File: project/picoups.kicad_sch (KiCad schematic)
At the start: 21 parts, among them J1 Conn_02x20_Odd_Even, J2 Conn_01x02, J3 Conn_01x02, SW1 SW_Push

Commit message: Cleanup
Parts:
- removed C1: 1uF, Capacitor_SMD:C_0603_1608Metric, symbol Device:C
- removed C2, C4: 22uF, Capacitor_SMD:C_0805_2012Metric, symbol Device:C
- removed C3: 47nF, Capacitor_SMD:C_0603_1608Metric, symbol Device:C
- removed C5, C6: 10uF, Capacitor_SMD:C_0603_1608Metric, symbol Device:C
- removed D1: LED, LED_SMD:LED_0805_2012Metric, symbol Device:LED
- removed J2, J3: Conn_01x02, Connector_JST:JST_PH_S2B-PH-K_1x02_P2.00mm_Horizontal, symbol Connector_Generic:Conn_01x02
- removed L1: 10uH, PicoUPS:Inductor, symbol Device:L
- removed R1: 240k, Resistor_SMD:R_0201_0603Metric, symbol Device:R
- removed R2, R3: R, Resistor_SMD:R_0201_0603Metric, symbol Device:R
- removed R4, R5: 10k, Resistor_SMD:R_0201_0603Metric, symbol Device:R
- removed SW1: SW_Push, Button_Switch_SMD:SW_Push_1P1T_NO_Vertical_Wuerth_434133025816, symbol Switch:SW_Push
- removed TH1: Thermistor_NTC, Connector_PinHeader_2.54mm:PinHeader_1x02_P2.54mm_Vertical, symbol Device:Thermistor_NTC
- removed TP1: DP, TestPoint:TestPoint_Pad_D1.5mm, symbol Connector:TestPoint
- removed TP2: DM, TestPoint:TestPoint_Pad_D1.5mm, symbol Connector:TestPoint
- removed U2: ~, PicoUPS:MP2731, symbol PicoUPS:MP2731
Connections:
- removed net GNDA: J1.14 (Pin_14), J1.20 (Pin_20), J1.25 (Pin_25), J1.30 (Pin_30), J1.34 (Pin_34), J1.39 (Pin_39), J1.6 (Pin_6), J1.9 (Pin_9)
- net INT: no longer names the net of J1.11 (Pin_11)
- net OTG: no longer names the net of J1.15 (Pin_15)
- net SCL: no longer names the net of J1.5 (Pin_5)
- net SDA: no longer names the net of J1.3 (Pin_3)
- net ~{CE}: no longer names the net of J1.13 (Pin_13)
- no-connect marks 27 -> 0

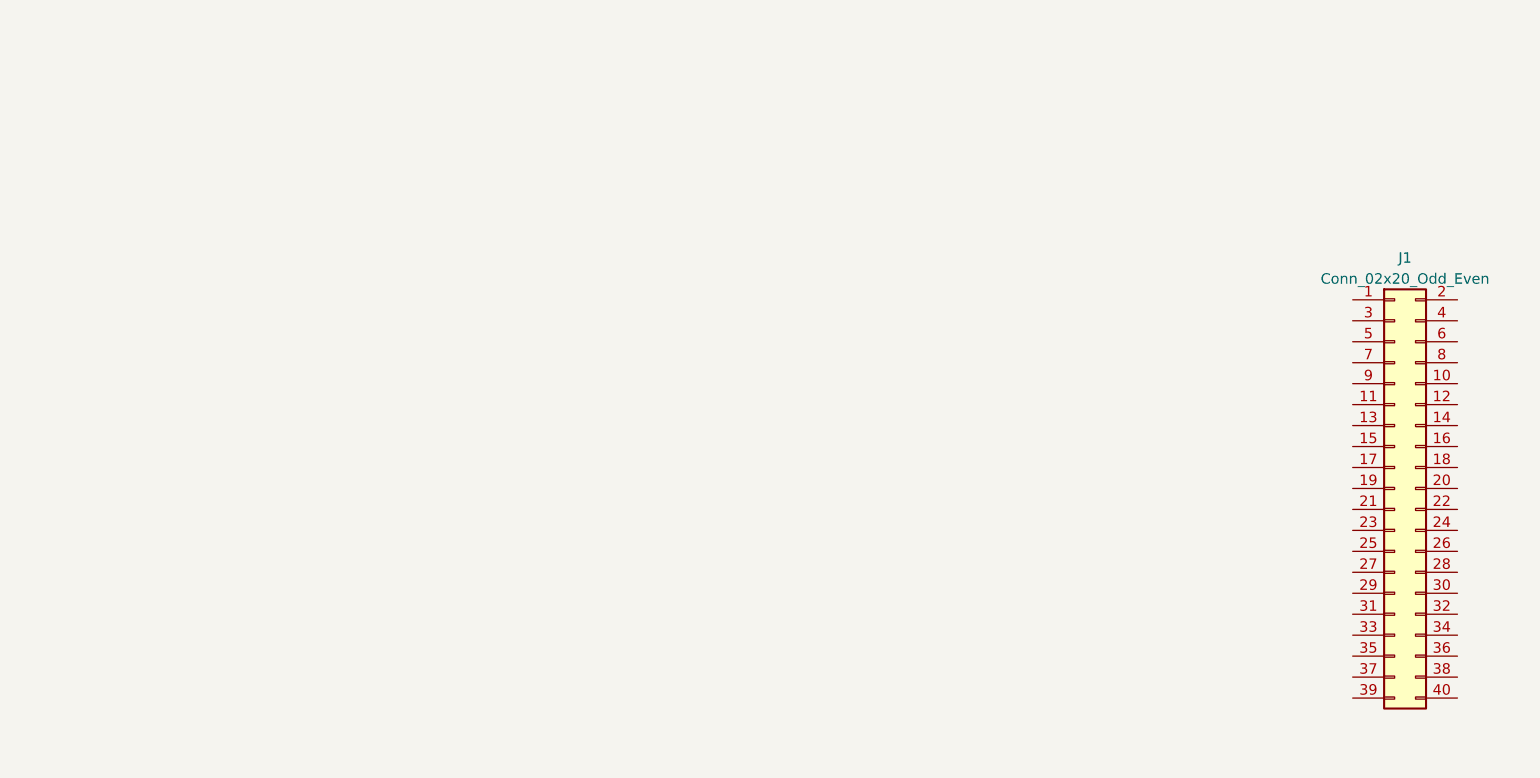
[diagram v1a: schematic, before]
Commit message: Created basic schematic
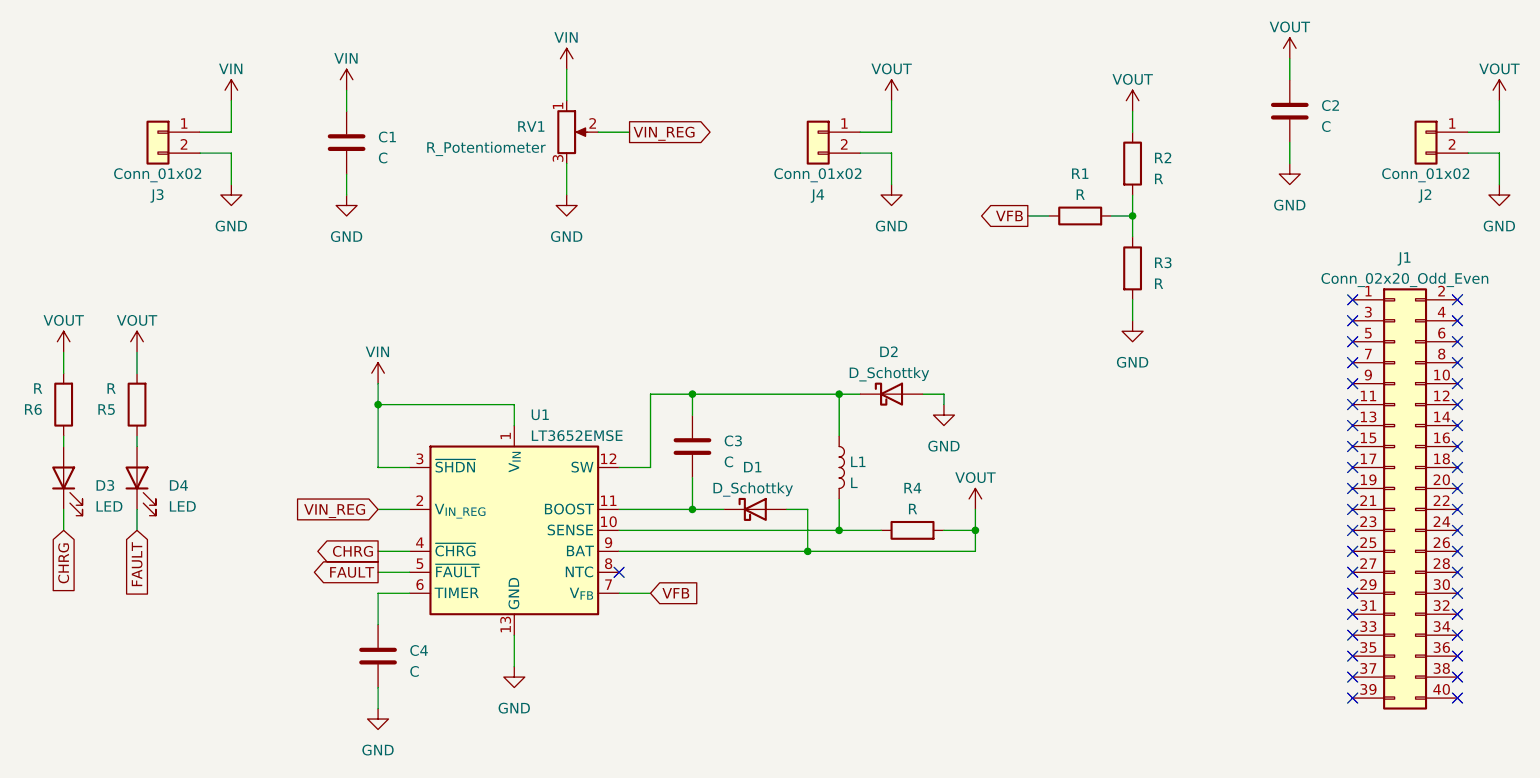
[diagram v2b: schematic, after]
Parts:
- added C1, C2, C3, C4: C, Capacitor_SMD:C_0805_2012Metric, symbol Device:C
- added D1, D2: D_Schottky, Diode_SMD:D_0805_2012Metric, symbol Device:D_Schottky
- added D3, D4: LED, LED_SMD:LED_0805_2012Metric, symbol Device:LED
- added J2: Conn_01x02, Connector_JST:JST_PH_B2B-PH-K_1x02_P2.00mm_Vertical, symbol Connector_Generic:Conn_01x02
- added J3, J4: Conn_01x02, Connector_JST:JST_PH_S2B-PH-K_1x02_P2.00mm_Horizontal, symbol Connector_Generic:Conn_01x02
- added L1: L, PicoUPS:Inductor, symbol Device:L
- added R1, R2, R3, R4, R5, R6: R, Resistor_SMD:R_0805_2012Metric, symbol Device:R
- added RV1: R_Potentiometer, Potentiometer_SMD:Potentiometer_Bourns_3214G_Horizontal, symbol Device:R_Potentiometer
- added U1: LT3652EMSE, Package_SO:MSOP-12-1EP_3x4mm_P0.65mm_EP1.65x2.85mm, symbol Battery_Management:LT3652EMSE
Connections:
- new net: L1.2, R4.1, U1.10 (SENSE)
- new net: D3.2 (A), R6.1
- new net: D4.2 (A), R5.1
- new net: C3.1, D2.1 (K), L1.1, U1.12 (SW)
- new net: C3.2, D1.1 (K), U1.11 (BOOST)
- new net: U1.1 (V_{IN}), U1.3 (~{SHDN})
- new net: C4.1, U1.6 (TIMER)
- new net: R1.2, R2.2, R3.1
- new net CHRG: D3.1 (K), U1.4 (~{CHRG})
- new net FAULT: D4.1 (K), U1.5 (~{FAULT})
- new net VFB: R1.1, U1.7 (V_{FB})
- new net VIN_REG: RV1.2, U1.2 (V_{IN_REG})
- new net VOUT: C2.1, D1.2 (A), J2.1 (Pin_1), J4.1 (Pin_1), R2.1, R4.2, R5.2, R6.2, U1.9 (BAT)
- no-connect marks 0 -> 41

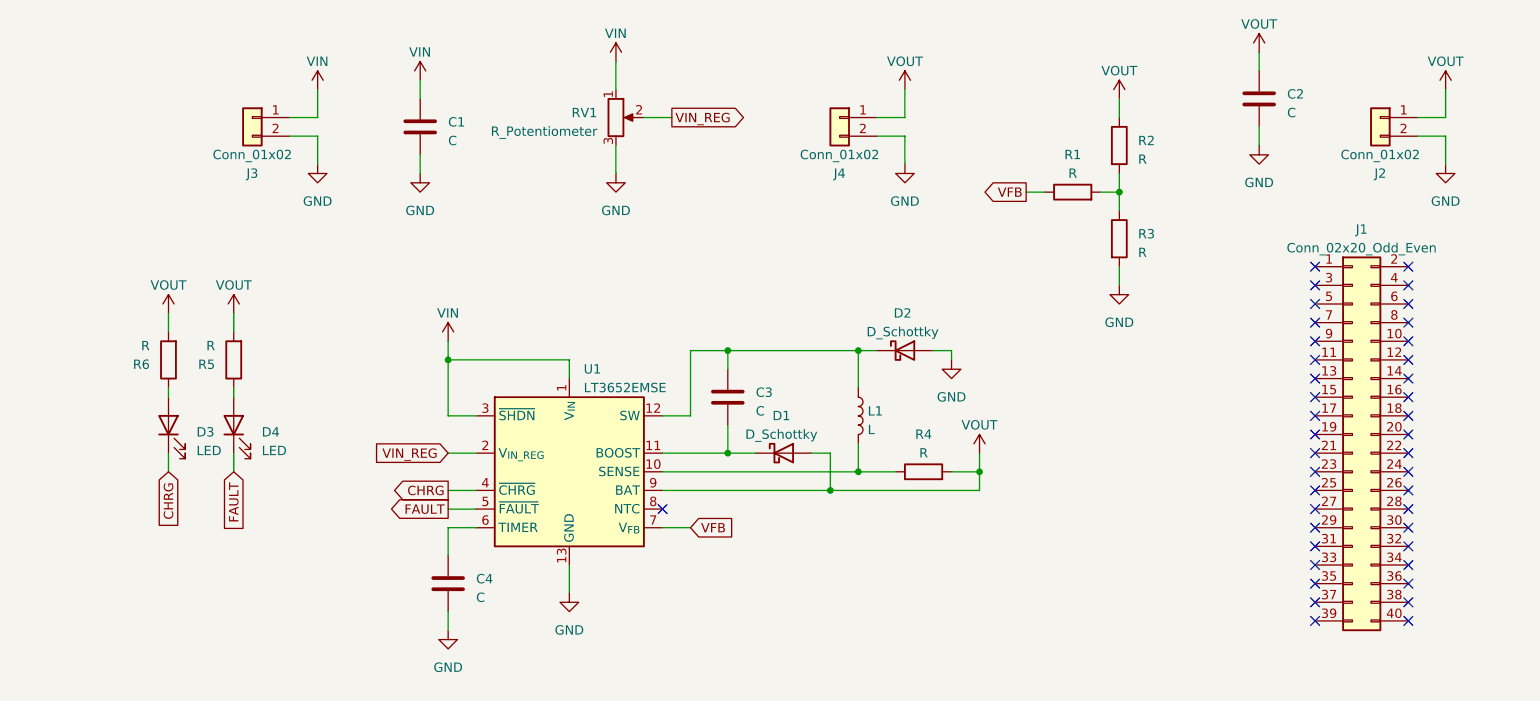
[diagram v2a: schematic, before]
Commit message: Added values and footprints
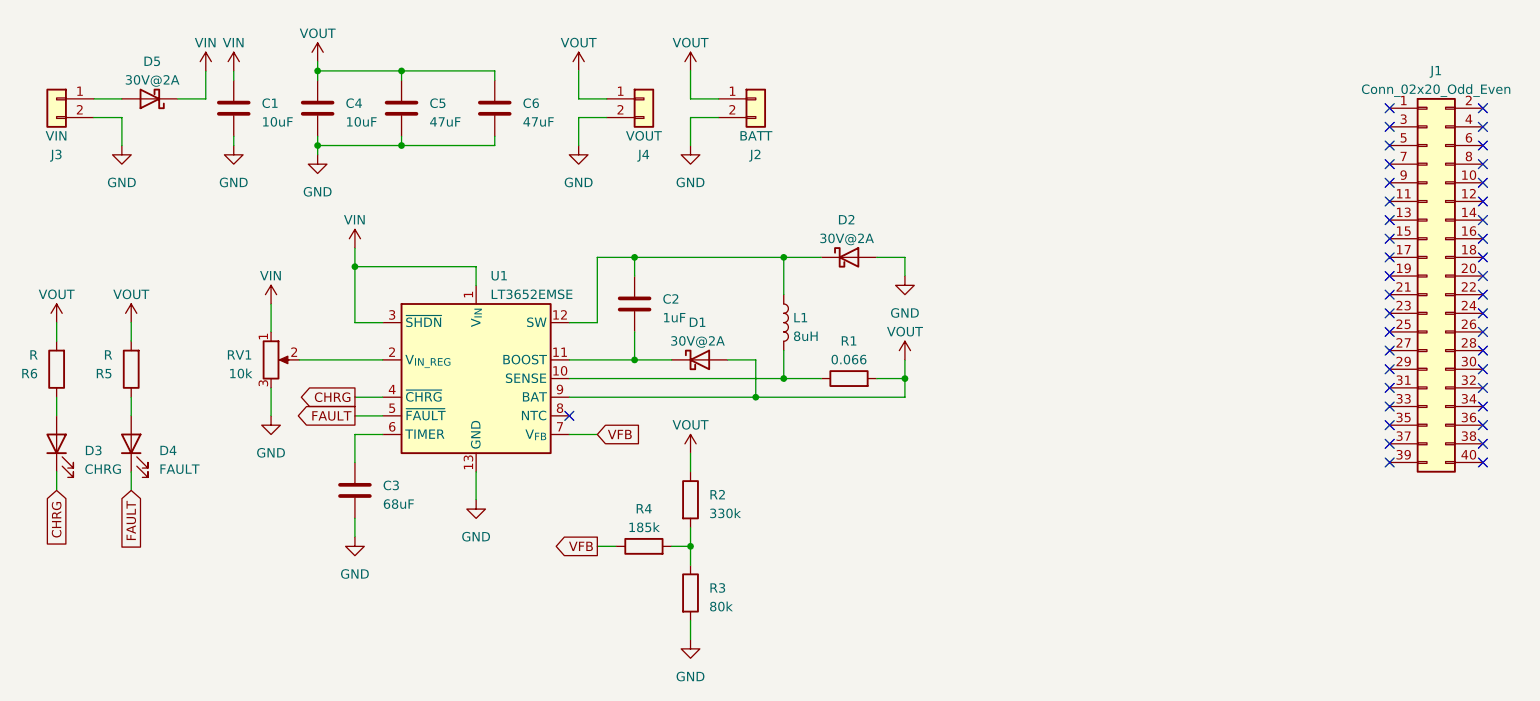
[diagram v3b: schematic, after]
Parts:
- added C5, C6: 47uF, Capacitor_SMD:C_1210_3225Metric, symbol Device:C
- added D5: 30V@2A, Diode_SMD:D_SMA, symbol Device:D_Schottky
- C1: value C -> 10uF
- C2: renamed from C3; value C -> 1uF
- C3: renamed from C4; value C -> 68uF
- C4: renamed from C2; value C -> 10uF
- D1, D2: value D_Schottky -> 30V@2A; footprint Diode_SMD:D_0805_2012Metric -> Diode_SMD:D_SMA
- D3: value LED -> CHRG
- D4: value LED -> FAULT
- J2: value Conn_01x02 -> BATT
- J3: value Conn_01x02 -> VIN
- J4: value Conn_01x02 -> VOUT
- L1: value L -> 8uH
- R1: renamed from R4; value R -> 0.066
- R2: value R -> 330k
- R3: value R -> 80k
- R4: renamed from R1; value R -> 185k
- RV1: value R_Potentiometer -> 10k
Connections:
- net VOUT: now also C5.1, C6.1
- net at C4.2: now also C5.2, C6.2
- net at J3.1 (Pin_1): now also D5.2 (A)
- net VIN_REG: no longer names the net of RV1.2, U1.2 (V_{IN_REG})
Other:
- moved on the sheet: C1, C2, C3, C4, D1, D2, D3, D4, J1, J2, J3, J4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

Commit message: First board prototype
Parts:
- added TP1: VIN_REG, TestPoint:TestPoint_Pad_D2.0mm, symbol Connector:TestPoint
- added TP2: GND, TestPoint:TestPoint_Pad_D2.0mm, symbol Connector:TestPoint
- J2: footprint Connector_JST:JST_PH_B2B-PH-K_1x02_P2.00mm_Vertical -> Connector_JST:JST_PH_S2B-PH-K_1x02_P2.00mm_Horizontal
- J4: footprint Connector_JST:JST_PH_S2B-PH-K_1x02_P2.00mm_Horizontal -> Connector_JST:JST_PH_B2B-PH-K_1x02_P2.00mm_Vertical
- RV1: footprint Potentiometer_SMD:Potentiometer_Bourns_3214G_Horizontal -> PicoUPS:Potentiometer_Bourns_3214G_Horizontal
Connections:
- net VIN: now reaches D5.1 (K)
- net VIN: now also C1.1, RV1.1, U1.1 (V_{IN}), U1.3 (~{SHDN})
- net RAW: now reaches D5.2 (A), J3.1 (Pin_1)
- net SENSE: now reaches L1.2, R1.1, U1.10 (SENSE)
- net GND: now reaches J2.2 (Pin_2)
- net GND: now also C1.2, C3.2, C4.2, C5.2, C6.2, D2.2 (A), J3.2 (Pin_2), J4.2 (Pin_2), R3.2, RV1.3, U1.13 (GND), TP2.1
- net SW: now reaches C2.1, D2.1 (K), L1.1, U1.12 (SW)
- net BOOST: now reaches C2.2, D1.1 (K), U1.11 (BOOST)
- net VIN_REG: now reaches RV1.2, U1.2 (V_{IN_REG})
- net VIN_REG: now also TP1.1
- net TIMER: now reaches C3.1, U1.6 (TIMER)
- net VOUT renamed VBAT
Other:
- moved on the sheet: C3, D5, J3, R2, R3, R4

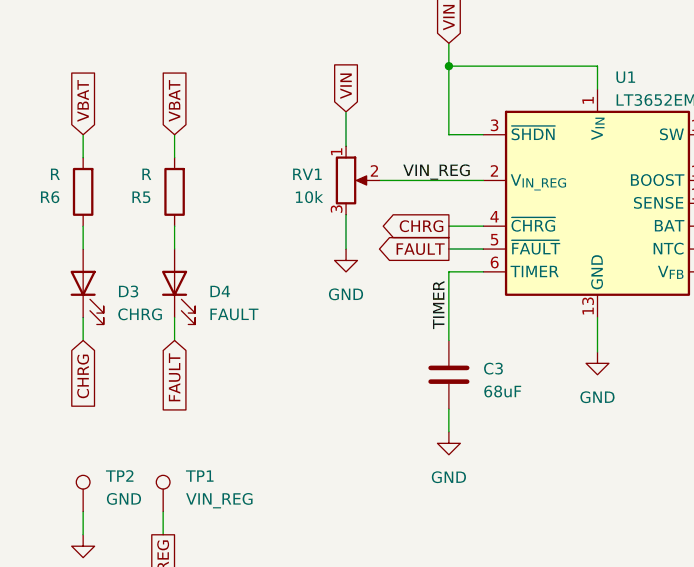
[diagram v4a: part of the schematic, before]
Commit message: Rearrange based on available parts
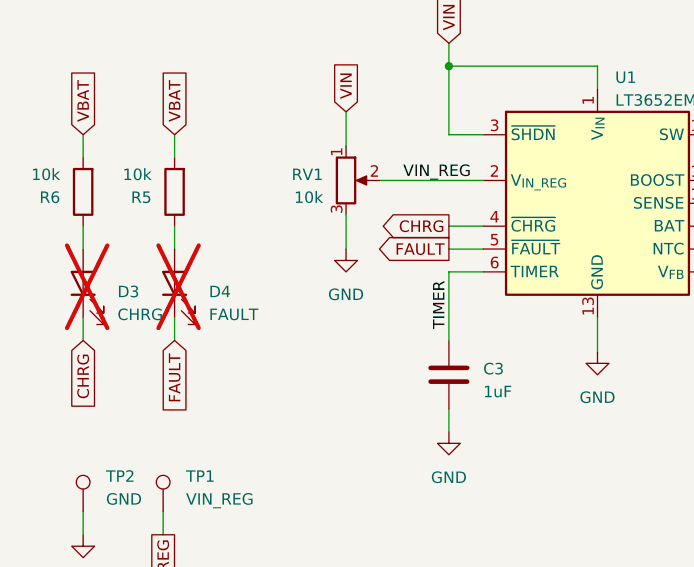
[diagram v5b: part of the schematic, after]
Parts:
- C1, C4: footprint Capacitor_SMD:C_0805_2012Metric -> Capacitor_SMD:C_1206_3216Metric
- C3: value 68uF -> 1uF
- D1, D2, D5: footprint Diode_SMD:D_SMA -> Diode_SMD:D_MicroSMP_AK
- D3, D4: now not fitted
- L1: footprint PicoUPS:Inductor -> Inductor_SMD:L_Wuerth_HCI-1050
- R5, R6: value R -> 10k
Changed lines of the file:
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@@
       (effects (font (size 1.27 1.27)))
     )
-    (property "Footprint" "Diode_SMD:D_SMA" (at 36.83 27.94 0)
+    (property "Footprint" "Diode_SMD:D_MicroSMP_AK" (at 36.83 27.94 0)
       (effects (font (size 1.27 1.27)) hide)
     )
@@
   )
   (symbol (lib_id "Device:LED") (at 26.67 74.93 90) (unit 1)
-    (in_bom yes) (on_board yes) (dnp no) (fields_autoplaced)
+    (in_bom yes) (on_board yes) (dnp yes) (fields_autoplaced)
     (property "Reference" "D3" (at 30.48 75.8825 90)
       (effects (font (size 1.27 1.27)) (justify right))
@@
       (effects (font (size 1.27 1.27)) (justify left))
     )
-    (property "Value" "R" (at 34.29 62.865 0)
+    (property "Value" "10k" (at 34.29 62.865 0)
       (effects (font (size 1.27 1.27)) (justify left))
     )
@@
       (effects (font (size 1.27 1.27)))
     )
-    (property "Footprint" "Diode_SMD:D_SMA" (at 134.62 49.53 0)
+    (property "Footprint" "Diode_SMD:D_MicroSMP_AK" (at 134.62 49.53 0)
       (effects (font (size 1.27 1.27)) hide)
     )
@@
       (effects (font (size 1.27 1.27)) (justify left))
     )
-    (property "Footprint" "Capacitor_SMD:C_0805_2012Metric" (at 51.7652 33.02 0)
+    (property "Footprint" "Capacitor_SMD:C_1206_3216Metric" (at 51.7652 33.02 0)
       (effects (font (size 1.27 1.27)) hide)
     )
@@
       (effects (font (size 1.27 1.27)))
     )
-    (property "Footprint" "Diode_SMD:D_SMA" (at 114.3 63.5 0)
+    (property "Footprint" "Diode_SMD:D_MicroSMP_AK" (at 114.3 63.5 0)
       (effects (font (size 1.27 1.27)) hide)
     )
@@
   )
   (symbol (lib_id "Device:LED") (at 36.83 74.93 90) (unit 1)
-    (in_bom yes) (on_board yes) (dnp no) (fields_autoplaced)
+    (in_bom yes) (on_board yes) (dnp yes) (fields_autoplaced)
     (property "Reference" "D4" (at 40.64 75.8825 90)
       (effects (font (size 1.27 1.27)) (justify right))
@@
       (effects (font (size 1.27 1.27)) (justify left))
     )
-    (property "Footprint" "Capacitor_SMD:C_0805_2012Metric" (at 63.1952 33.02 0)
+    (property "Footprint" "Capacitor_SMD:C_1206_3216Metric" (at 63.1952 33.02 0)
       (effects (font (size 1.27 1.27)) hide)
     )
@@
       (effects (font (size 1.27 1.27)) (justify left))
     )
-    (property "Value" "R" (at 24.13 62.865 0)
+    (property "Value" "10k" (at 24.13 62.865 0)
       (effects (font (size 1.27 1.27)) (justify left))
     )
@@
       (effects (font (size 1.27 1.27)) (justify left))
     )
-    (property "Footprint" "PicoUPS:Inductor" (at 125.73 58.42 0)
+    (property "Footprint" "Inductor_SMD:L_Wuerth_HCI-1050" (at 125.73 58.42 0)
       (effects (font (size 1.27 1.27)) hide)
     )
@@
       (effects (font (size 1.27 1.27)) (justify left))
     )
-    (property "Value" "68uF" (at 71.12 86.995 0)
-      (effects (font (size 1.27 1.27)) (justify left))
-    )
+    (property "Value" "1uF" (at 71.12 86.995 0)
+      (effects (font (size 1.27 1.27)) (justify left))
+    )

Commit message: Fixed incorrect VIN_REG divider
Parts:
- R2: value 330k -> 80k
- R3: value 80k -> 330k
- R5, R6: value 10k -> 260
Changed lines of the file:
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@@
       (effects (font (size 1.27 1.27)) (justify left))
     )
-    (property "Value" "10k" (at 34.29 62.865 0)
+    (property "Value" "260" (at 34.29 62.865 0)
       (effects (font (size 1.27 1.27)) (justify left))
     )
@@
   (symbol (lib_id "Device:R") (at 115.57 76.2 0) (unit 1)
     (in_bom yes) (on_board yes) (dnp no) (fields_autoplaced)
-    (property "Reference" "R2" (at 118.11 75.565 0)
-      (effects (font (size 1.27 1.27)) (justify left))
-    )
-    (property "Value" "330k" (at 118.11 78.105 0)
+    (property "Reference" "R2" (at 118.11 74.93 0)
+      (effects (font (size 1.27 1.27)) (justify left))
+    )
+    (property "Value" "80k" (at 118.11 77.47 0)
       (effects (font (size 1.27 1.27)) (justify left))
     )
@@
       (effects (font (size 1.27 1.27)) (justify left))
     )
-    (property "Value" "10k" (at 24.13 62.865 0)
+    (property "Value" "260" (at 24.13 62.865 0)
       (effects (font (size 1.27 1.27)) (justify left))
     )
@@
   (symbol (lib_id "Device:R") (at 115.57 88.9 0) (unit 1)
     (in_bom yes) (on_board yes) (dnp no) (fields_autoplaced)
-    (property "Reference" "R3" (at 118.11 88.265 0)
-      (effects (font (size 1.27 1.27)) (justify left))
-    )
-    (property "Value" "80k" (at 118.11 90.805 0)
-      (effects (font (size 1.27 1.27)) (justify left))
-    )
+    (property "Reference" "R3" (at 118.11 87.63 0)
+      (effects (font (size 1.27 1.27)) (justify left))
+    )
+    (property "Value" "330k" (at 118.11 90.17 0)
+      (effects (font (size 1.27 1.27)) (justify left))
+    )
